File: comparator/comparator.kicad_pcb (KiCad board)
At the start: 4 copper layers, 55.9 x 22.9 mm, 54 parts, among them J1 PMOD, J10 SMA, J11 DC Block, J12 50R Term/Ref, J20 SMA, J21 DC Block, J22 50R Term/Ref, U30 LT1711xMS8, U40 LM2776, U51 LM4040DBZ-2.5, U52 LM4040DBZ-2.5

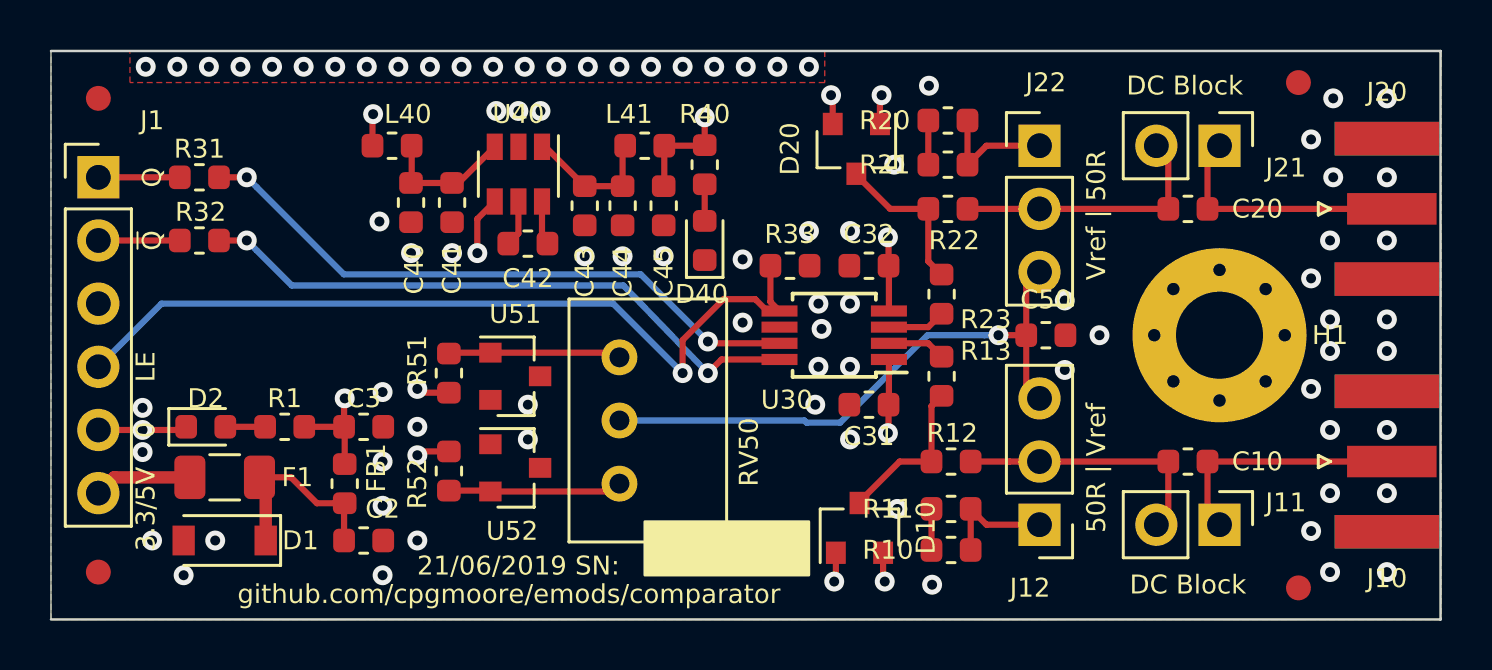
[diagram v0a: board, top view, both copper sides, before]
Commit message: Powerplane rearranged
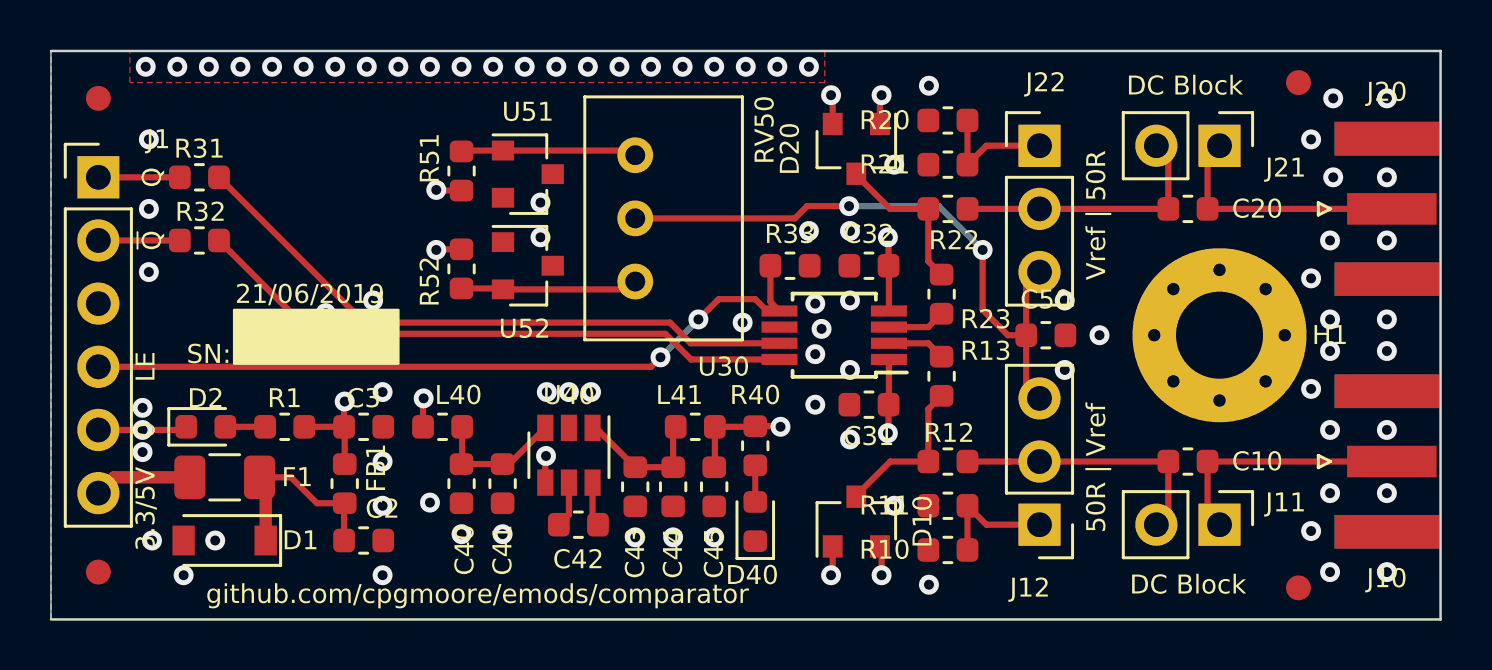
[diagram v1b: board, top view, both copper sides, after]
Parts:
- moved C40 11.5 mm to (138.4, 103.8)
- moved C45 11.5 mm to (148.6, 103.9)
- moved D40 11.5 mm to (150.2, 105.3)
- moved L40 11.5 mm to (137.7, 101.5)
- moved L41 11.5 mm to (147.8, 101.5)
- moved R40 11.5 mm to (150.2, 102.2)
- moved C41 11.5 mm to (140.1, 103.8)
- moved C42 11.5 mm to (143.1, 105.4)
- moved C43 11.5 mm to (145.4, 103.9)
- moved C44 11.5 mm to (146.9, 103.9)
- moved U40 11.5 mm to (142.7, 102.6)
- moved RV50 8.15 mm to (145.4, 90.6)
- moved R52 8.14 mm to (138.4, 95.1)
- moved U51 8.14 mm to (141.1, 91.3)
- moved U52 8.14 mm to (141.1, 95.0)
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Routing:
- net /VCC_P: track 14.8 -> 77.6 mm
- net /VCC_N: track 11.1 -> 65.8 mm
- net GND: track 7.01 -> 3.58 mm, vias 83 -> 86
- net /LE: track 33.8 -> 30.7 mm, vias 1 -> 2
- net /V_REF: track 23.4 -> 25.0 mm, vias 1 -> 2
- net /~Q: track 25.0 -> 24.5 mm, vias 2 -> 0
- net /Q: vias 2 -> 0
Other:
- board text added: "21/06/2019"
- board text added: "SN:"
- board text removed: "21/06/2019 SN:"
